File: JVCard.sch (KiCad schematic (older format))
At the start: 75 parts, among them J6 Conn_02x25_Odd_Even, Q1 mmbt3904, Q2 mmbt3904, Q3 mmbt3904, Q4 mmbt3904, Q5 mmbt3904, Q6 mmbt3904, U4 SCART_CONN, U5 MET1117A50B3G

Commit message: fixed regularot pinout whoops
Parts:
- removed U5: MET1117A50B3G, Package_TO_SOT_SMD:SOT-223-3_TabPin2, symbol Regulator_Linear:L78L12_SOT89
- added U1: AMS1117-5.0, Package_TO_SOT_SMD:SOT-223-3_TabPin2, symbol Regulator_Linear:AMS1117-5.0
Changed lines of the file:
@@
-$EndComp
-$Comp
-L Regulator_Linear:L78L12_SOT89 U5
-U 1 1 5DC85F25
-P 2650 6650
-F 0 "U5" H 2650 6892 50  0000 C CNN
-F 1 "MET1117A50B3G" H 2650 6801 50  0000 C CNN
-F 2 "Package_TO_SOT_SMD:SOT-223-3_TabPin2" H 2650 6850 50  0001 C CIN
-F 3 "" H 2650 6600 50  0001 C CNN
-F 4 " C83973" H 2650 6650 50  0001 C CNN "LCSC"
-	1    2650 6650
-	1    0    0    -1
 $EndComp
 $Comp
@@
 Wire Wire Line
 	2950 6650 3250 6650
+Connection ~ 3250 6650
+$Comp
+L Regulator_Linear:AMS1117-5.0 U1
+U 1 1 5E7E5356
+P 2650 6650
+F 0 "U1" H 2650 6892 50  0000 C CNN
+F 1 "AMS1117-5.0" H 2650 6801 50  0000 C CNN
+F 2 "Package_TO_SOT_SMD:SOT-223-3_TabPin2" H 2650 6850 50  0001 C CNN
+F 3 "http://www.advanced-monolithic.com/pdf/ds1117.pdf" H 2750 6400 50  0001 C CNN
+	1    2650 6650
+	1    0    0    -1
+$EndComp
 Connection ~ 2950 6650
-Connection ~ 3250 6650
 $EndSCHEMATC

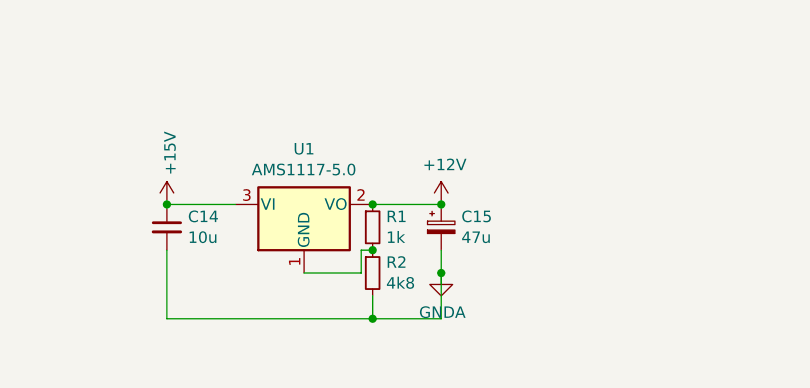
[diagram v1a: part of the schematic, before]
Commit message: fix resistor too
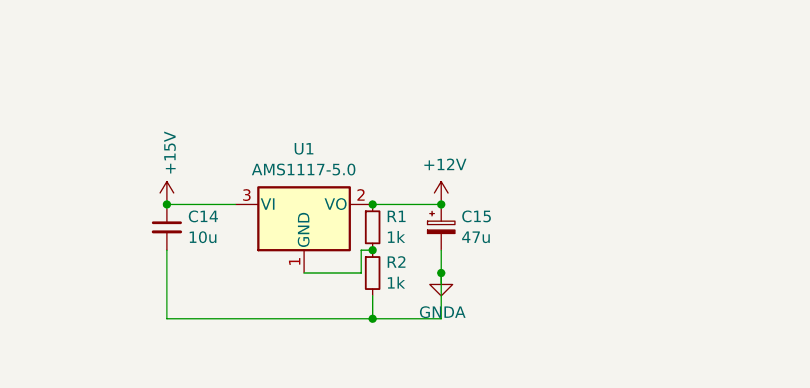
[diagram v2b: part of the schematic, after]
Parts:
- R2: value 4k8 -> 1k; LCSC C17676 -> C17513
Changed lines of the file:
@@
 P 2950 6950
 F 0 "R2" H 3009 6996 50  0000 L CNN
-F 1 "4k8" H 3009 6905 50  0000 L CNN
+F 1 "1k" H 3009 6905 50  0000 L CNN
 F 2 "Resistor_SMD:R_0805_2012Metric_Pad1.15x1.40mm_HandSolder" H 2950 6950 50  0001 C CNN
 F 3 "~" H 2950 6950 50  0001 C CNN
-F 4 "C17676" H 2950 6950 50  0001 C CNN "LCSC"
+F 4 "C17513" H 2950 6950 50  0001 C CNN "LCSC"
 	1    2950 6950
 	1    0    0    -1

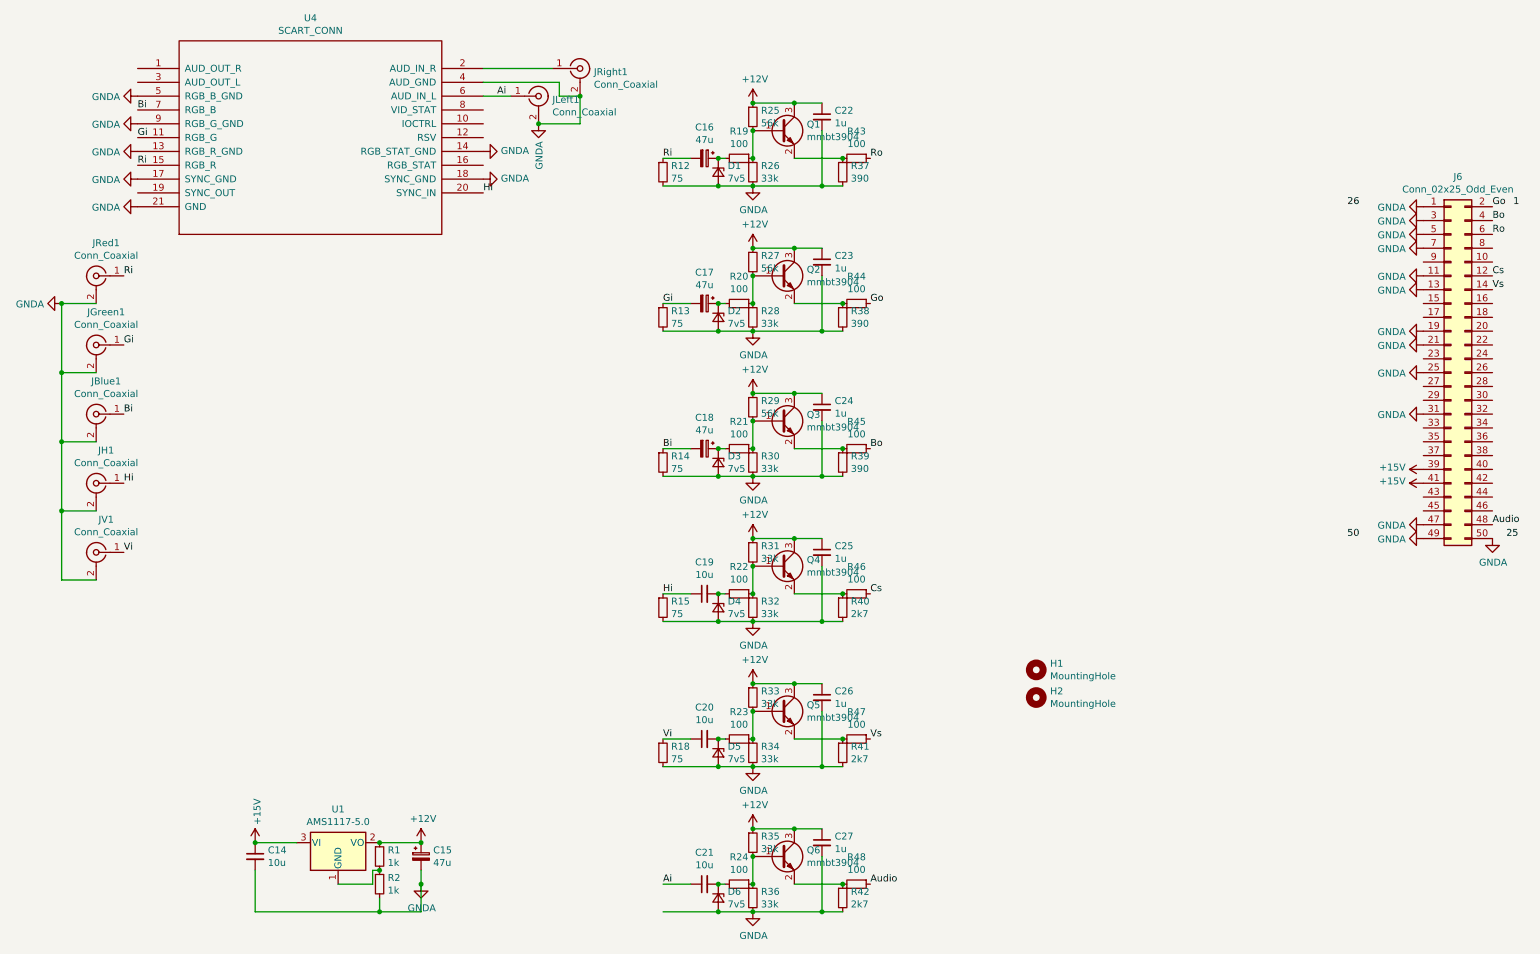
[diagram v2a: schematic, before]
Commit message: draft scart-vga inside
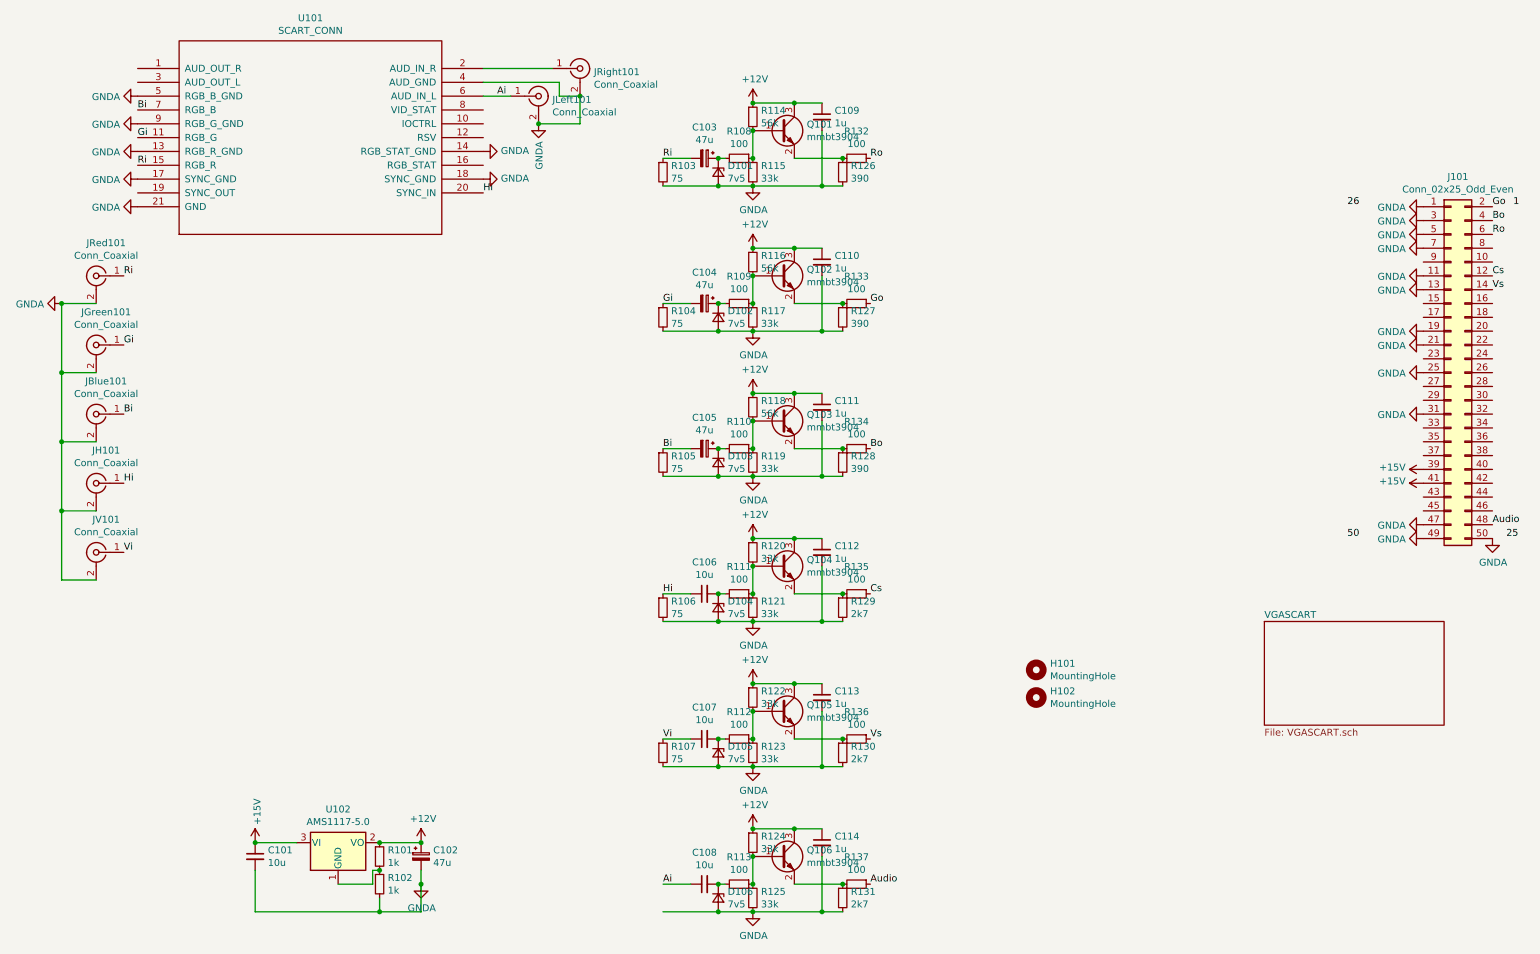
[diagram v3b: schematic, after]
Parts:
- JBlue101: renamed from JBlue1; footprint Connector_Coaxial:BNC_Amphenol_B6252HB-NPP3G-50_Horizontal -> videobits:BNC_Amphenol_B6252HB-NPP3G-50_Horizontal_smallerpads
- JGreen101: renamed from JGreen1; footprint Connector_Coaxial:BNC_Amphenol_B6252HB-NPP3G-50_Horizontal -> videobits:BNC_Amphenol_B6252HB-NPP3G-50_Horizontal_smallerpads
- JH101: renamed from JH1; footprint Connector_Coaxial:BNC_Amphenol_B6252HB-NPP3G-50_Horizontal -> videobits:BNC_Amphenol_B6252HB-NPP3G-50_Horizontal_smallerpads
- JRed101: renamed from JRed1; footprint Connector_Coaxial:BNC_Amphenol_B6252HB-NPP3G-50_Horizontal -> videobits:BNC_Amphenol_B6252HB-NPP3G-50_Horizontal_smallerpads
- JV101: renamed from JV1; footprint Connector_Coaxial:BNC_Amphenol_B6252HB-NPP3G-50_Horizontal -> videobits:BNC_Amphenol_B6252HB-NPP3G-50_Horizontal_smallerpads
- renumbered C14 to C101, C15 to C102, C16 to C103, C17 to C104, C18 to C105, C19 to C106, C20 to C107, C21 to C108, C22 to C109, C23 to C110, C24 to C111, C25 to C112, C26 to C113, C27 to C114, D1 to D101, D2 to D102, D3 to D103, D4 to D104, D5 to D105, D6 to D106, H1 to H101, H2 to H102, J6 to J101, JLeft1 to JLeft101, JRight1 to JRight101, Q1 to Q101, Q2 to Q102, Q3 to Q103, Q4 to Q104, Q5 to Q105, Q6 to Q106, R1 to R101, R2 to R102, R12 to R103, R13 to R104, R14 to R105, R15 to R106, R18 to R107, R19 to R108, R20 to R109, R21 to R110, R22 to R111, R23 to R112, R24 to R113, R25 to R114, R26 to R115, R27 to R116, R28 to R117, R29 to R118, R30 to R119, R31 to R120, R32 to R121, R33 to R122, R34 to R123, R35 to R124, R36 to R125, R37 to R126, R38 to R127, R39 to R128, R40 to R129, R41 to R130, R42 to R131, R43 to R132, R44 to R133, R45 to R134, R46 to R135, R47 to R136, R48 to R137, U4 to U101, U1 to U102
